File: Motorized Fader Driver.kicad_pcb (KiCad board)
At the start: 2 copper layers, 0 parts

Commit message: Update PCB
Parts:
- added C10: 100n, Capacitor_SMD:C_0402_1005Metric, B.Cu at (82.7, 38.4)
- added C11: 1u, Capacitor_SMD:C_0402_1005Metric, B.Cu at (79.8, 30.5)
- added C12: 100n, Capacitor_SMD:C_0402_1005Metric, B.Cu at (79.8, 32.5)
- added C13: 1u, Capacitor_SMD:C_0402_1005Metric, B.Cu at (79.8, 34.4)
- added C14: 100n, Capacitor_SMD:C_0402_1005Metric, B.Cu at (79.8, 36.4)
- added C15: 100n, Capacitor_SMD:C_0402_1005Metric, B.Cu at (79.8, 38.4)
- added C16: 100n, Capacitor_SMD:C_0402_1005Metric, B.Cu at (77.0, 30.5)
- added C17: 100n, Capacitor_SMD:C_0402_1005Metric, B.Cu at (77.0, 32.5)
- added C18: 100n, Capacitor_SMD:C_0402_1005Metric, B.Cu at (77.0, 34.4)
- added C19: 100n, Capacitor_SMD:C_0402_1005Metric, B.Cu at (77.0, 36.4)
- added C4: 15p, Capacitor_SMD:C_0402_1005Metric, B.Cu at (82.7, 30.5)
- added C5: 15p, Capacitor_SMD:C_0402_1005Metric, B.Cu at (82.7, 32.5)
- added C6: 10u, Capacitor_SMD:C_0805_2012Metric, B.Cu at (75.3, 49.6)
- added C7: 10u, Capacitor_SMD:C_0805_2012Metric, B.Cu at (75.3, 52.6)
- added C8: 100n, Capacitor_SMD:C_0402_1005Metric, B.Cu at (82.7, 34.4)
- added C9: 100n, Capacitor_SMD:C_0402_1005Metric, B.Cu at (82.7, 36.4)
- added J1: Conn_01x02, Connector_PinHeader_2.54mm:PinHeader_1x02_P2.54mm_Vertical, F.Cu at (110.5, 54.5)
- added J3: Conn_01x02, Connector_PinHeader_2.54mm:PinHeader_1x02_P2.54mm_Vertical, B.Cu at (89.0, 38.2)
- added R5: 1k, Resistor_SMD:R_0402_1005Metric, B.Cu at (82.7, 40.4)
- added R6: DNF, Resistor_SMD:R_0402_1005Metric, B.Cu at (82.7, 42.4)
- added R7: 1k, Resistor_SMD:R_0402_1005Metric, B.Cu at (82.7, 44.3)
- added R8: 27, Resistor_SMD:R_0402_1005Metric, B.Cu at (82.7, 46.3)
- added R9: 27, Resistor_SMD:R_0402_1005Metric, B.Cu at (82.7, 48.3)
- added U1: DRV8833PWP, Package_SO:HTSSOP-16-1EP_4.4x5mm_P0.65mm_EP3.4x5mm_Mask2.46x2.31mm_ThermalVias, B.Cu at (101.8, 48.0)
- added U4: NCP1117-3.3_SOT223, Package_TO_SOT_SMD:SOT-223-3_TabPin2, B.Cu at (32.5, 43.0)
- added U5: W25Q128JVS, Package_SO:SOIC-8_5.23x5.23mm_P1.27mm, B.Cu at (48.0, 45.0)
- added U6: RP2040, Package_DFN_QFN:QFN-56-1EP_7x7mm_P0.4mm_EP3.2x3.2mm_ThermalVias, B.Cu at (31.9, 32.4)
- added VR1: PSM60-081A-103B2, PSM60-081A-103B2:PSM60081A103B2, F.Cu at (110.1, 32.1)
- added Y2: ABM8-272-T3, Crystal:Crystal_SMD_3225-4Pin_3.2x2.5mm, B.Cu at (70.5, 50.3)
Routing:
- net Net-(J1-Pin_2): track 0.00 -> 14.4 mm
- net Net-(J1-Pin_1): track 0.00 -> 13.0 mm
- net /RP2040/GPIO6: track 0.00 -> 12.2 mm

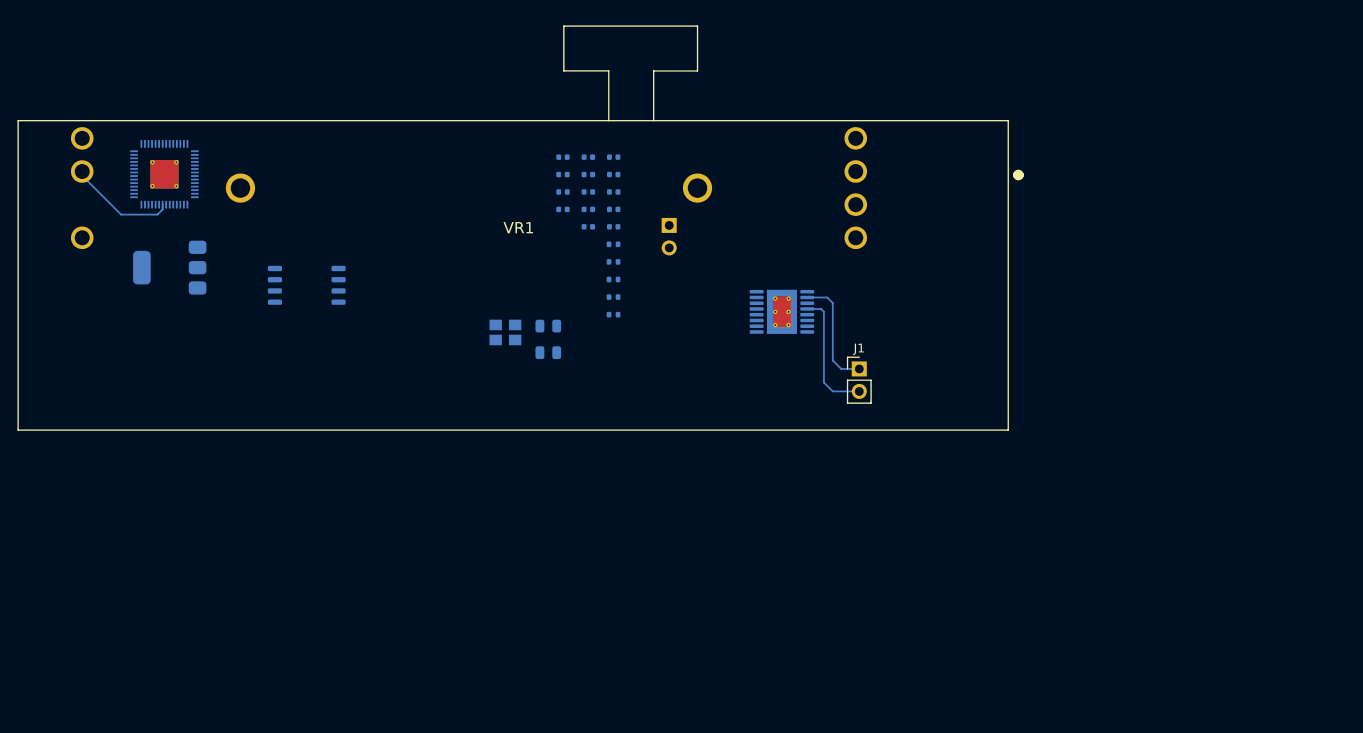
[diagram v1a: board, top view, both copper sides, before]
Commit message: Finish most of the schematic design
The majority of the schematic is in a pretty finalized state now. Also
some more work on the PCB has been done.
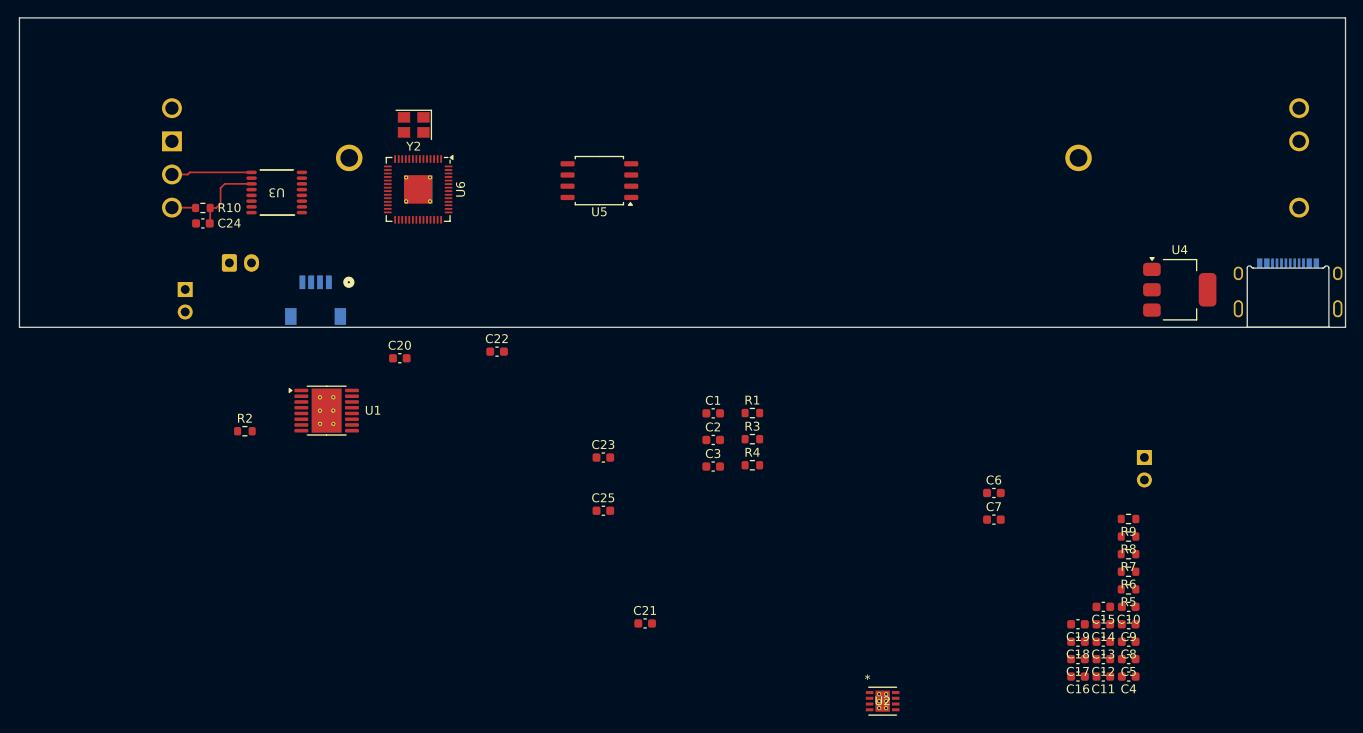
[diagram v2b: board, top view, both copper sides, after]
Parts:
- added C1: 2.2u, Capacitor_SMD:C_0603_1608Metric, F.Cu at (94.0, 59.5)
- added C2: 0.01u, Capacitor_SMD:C_0603_1608Metric, F.Cu at (94.0, 62.5)
- added C20: 0.1u, Capacitor_SMD:C_0603_1608Metric, F.Cu at (58.5, 53.2)
- added C21: 0.1u, Capacitor_SMD:C_0603_1608Metric, F.Cu at (86.3, 83.2)
- added C22: 0.1u, Capacitor_SMD:C_0603_1608Metric, F.Cu at (69.5, 52.5)
- added C23: 0.1u, Capacitor_SMD:C_0603_1608Metric, F.Cu at (81.5, 64.5)
- added C24: 100n, Capacitor_SMD:C_0603_1608Metric, F.Cu at (36.2, 38.0)
- added C25: 0.1u, Capacitor_SMD:C_0603_1608Metric, F.Cu at (81.5, 70.5)
- added C3: 10u, Capacitor_SMD:C_0603_1608Metric, F.Cu at (94.0, 65.5)
- added G***: LOGO, SparkFun-Qwiic:qwiic_6mm, B.Cu at (49.0, 42.0)
- added J2: Conn_I2C, Connector_SM04B_SRSS_TB:CONN_SM04B-SRSS-TB_JST, B.Cu at (49.0, 46.8)
- added J5: Conn_Mot_Pwr, Connector_JST:JST_EH_S2B-EH_1x02_P2.50mm_Horizontal, B.Cu at (39.2, 42.5)
- added J6: GSB1C4621DS1HR, GSB1C4621DS1HR:AMPHENOL_GSB1C4621DS1HR, B.Cu at (159.0, 47.6)
- added R1: 1M, Resistor_SMD:R_0603_1608Metric, F.Cu at (98.4, 59.5)
- added R10: 1k, Resistor_SMD:R_0603_1608Metric, F.Cu at (36.2, 36.2)
- added R2: 200m, Resistor_SMD:R_0603_1608Metric, F.Cu at (41.0, 61.5)
- added R3: 5.1k, Resistor_SMD:R_0603_1608Metric, F.Cu at (98.4, 62.4)
- added R4: 5.1k, Resistor_SMD:R_0603_1608Metric, F.Cu at (98.4, 65.3)
- added U2: TPS2115ADRBR, TPS2115ADRBR:DRB8_2P4X1P65, F.Cu at (113.1, 92.0)
- added U3: ADS1219IPWR, ADS1219IPWR:PW0016A_L, F.Cu at (44.6, 34.5)
- C10, C11, C12, C13, C14, C15, C16, C17, C18, C19, C4, C5, C8, C9: footprint Capacitor_SMD:C_0402_1005Metric -> Capacitor_SMD:C_0603_1608Metric; moved to F.Cu
- C6, C7: footprint Capacitor_SMD:C_0805_2012Metric -> Capacitor_SMD:C_0603_1608Metric; moved to F.Cu
- J1: value Conn_01x02 -> Conn_Mot; moved to B.Cu
- R5, R6, R7, R8, R9: footprint Resistor_SMD:R_0402_1005Metric -> Resistor_SMD:R_0603_1608Metric; moved to F.Cu
- U1, U4, U5, U6, Y2: moved to F.Cu
- VR1: value PSM60-081A-103B2 -> PSM01-081A-103B2; footprint PSM60-081A-103B2:PSM60081A103B2 -> PSM01-082A-103B2:PSM01081A103B2; moved to B.Cu
- moved U4 114.3 mm to (146.8, 45.5), turned to 0 degrees
- moved C11 82.7 mm to (138.1, 89.2)
- moved C16 82.7 mm to (135.2, 89.2)
- moved C4 82.7 mm to (141.0, 89.2)
- moved C17 80.0 mm to (135.2, 87.3)
- moved C12 80.0 mm to (138.1, 87.3)
- moved C5 80.0 mm to (141.0, 87.3)
- moved VR1 77.4 mm to (32.8, 28.7), turned to 180 degrees
- moved C18 77.3 mm to (135.2, 85.3)
- moved C13 77.3 mm to (138.1, 85.3)
- moved C8 77.3 mm to (141.0, 85.3)
- moved J1 76.8 mm to (34.2, 45.5), turned to 180 degrees
- moved C14 74.8 mm to (138.1, 83.3)
- moved C19 74.8 mm to (135.2, 83.3)
- moved C9 74.8 mm to (141.0, 83.3)
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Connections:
- net /RP2040/GPIO6 renamed /GPIO6
- U1 pad 1: unconnected-(U1-~{SLEEP}-Pad1) -> /RP2040/GPIO7
- U1 pad 10: unconnected-(U1-BIN2-Pad10) -> /RP2040/GPIO5
- U1 pad 11: unconnected-(U1-VCP-Pad11) -> Net-(U1-VCP)
- U1 pad 13: Net-(U1-GND-Pad13) -> GND
- U1 pad 14: unconnected-(U1-VINT-Pad14) -> Net-(U1-VINT)
- U1 pad 17: Net-(U1-GND-Pad13) -> GND
- U1 pad 3: unconnected-(U1-AISEN-Pad3) -> Net-(U1-AISEN)
- U1 pad 5: unconnected-(U1-BOUT2-Pad5) -> Net-(J1-Pin_2)
- U1 pad 6: unconnected-(U1-BISEN-Pad6) -> Net-(U1-AISEN)
- U1 pad 7: unconnected-(U1-BOUT1-Pad7) -> Net-(J1-Pin_1)
- U1 pad 8: unconnected-(U1-~{FAULT}-Pad8) -> /RP2040/GPIO8
- U1 pad 9: unconnected-(U1-BIN1-Pad9) -> /RP2040/GPIO4
- U4 pad 2: +3V3 -> Net-(U2-IN1)
- U6 pad 11: unconnected-(U6-GPIO8-Pad11) -> /RP2040/GPIO8
- U6 pad 2: unconnected-(U6-GPIO0-Pad2) -> /CONN_SDA
- U6 pad 3: unconnected-(U6-GPIO1-Pad3) -> /CONN_SCL
- U6 pad 38: /RP2040/ADC0 -> unconnected-(U6-GPIO26_ADC0-Pad38)
- U6 pad 4: unconnected-(U6-GPIO2-Pad4) -> /I2C_SDA
- U6 pad 5: unconnected-(U6-GPIO3-Pad5) -> /I2C_SCL
- U6 pad 9: unconnected-(U6-GPIO7-Pad9) -> /RP2040/GPIO7
- VR1 pad B2: /RP2040/ADC0 -> Net-(VR1-WIPER_2)
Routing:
- net Net-(J1-Pin_2): track 14.4 -> 0.00 mm
- net Net-(J1-Pin_1): track 13.0 -> 0.49 mm
- net /GPIO6: track 12.2 -> 0.00 mm
- net +3V3: track 0.00 -> 9.10 mm
- net Net-(U3-AIN0): track 0.00 -> 8.60 mm
- net Net-(VR1-WIPER_2): track 0.00 -> 2.69 mm
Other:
- board outline added: 150 x 35 mm

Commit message: Finish routing most of the PCB
The PCB should work now for the most part. Also fixes some miscellaneous
schematic things and swaps out a few components.
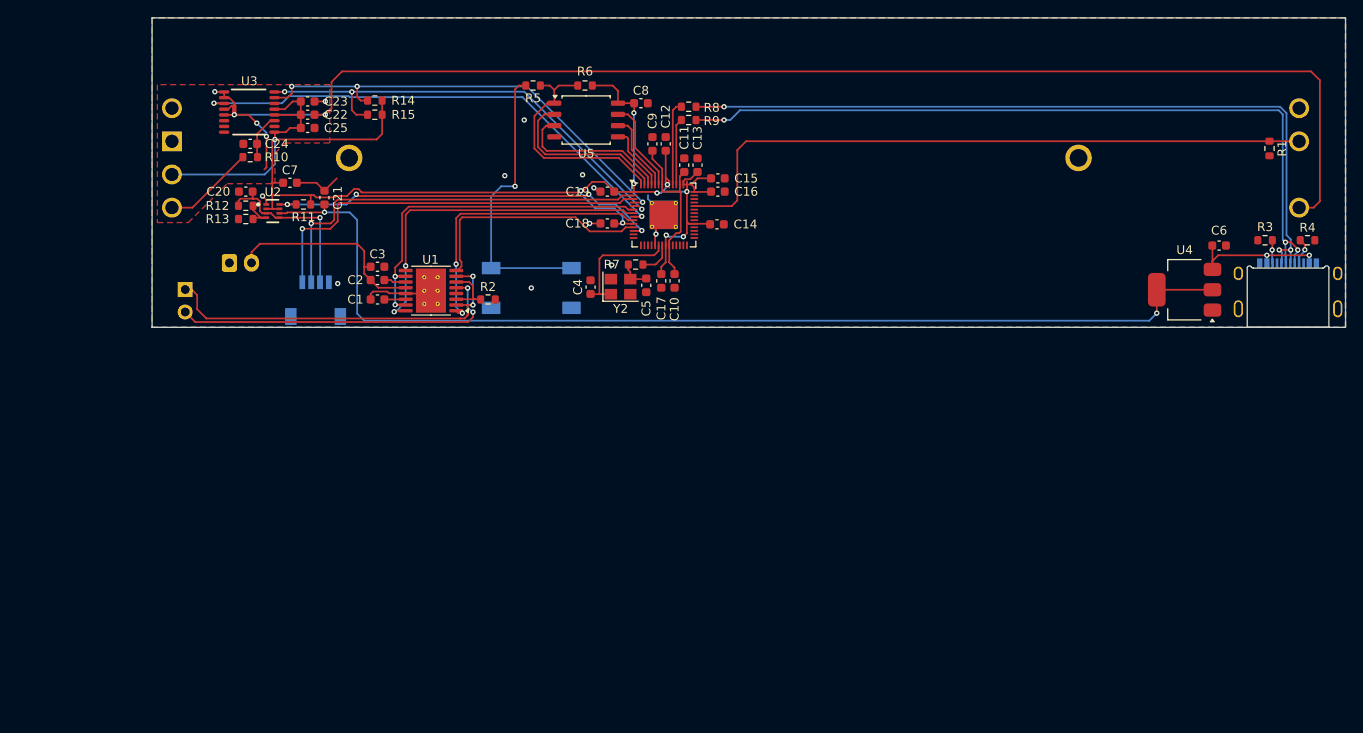
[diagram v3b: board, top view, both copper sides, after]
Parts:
- removed J3: Conn_01x02, Connector_PinHeader_2.54mm:PinHeader_1x02_P2.54mm_Vertical
- added NT1: NetTie_2, NetTie:NetTie-2_SMD_Pad0.5mm, F.Cu at (39.8, 25.2)
- added R11: R_Small, Resistor_SMD:R_0603_1608Metric, F.Cu at (47.6, 35.8)
- added R12: R_Small, Resistor_SMD:R_0603_1608Metric, F.Cu at (41.1, 36.0)
- added R13: R_Small, Resistor_SMD:R_0603_1608Metric, F.Cu at (41.1, 37.5)
- added R14: 4.7k, Resistor_SMD:R_0603_1608Metric, F.Cu at (55.7, 24.1)
- added R15: 4.7k, Resistor_SMD:R_0603_1608Metric, F.Cu at (55.7, 25.7)
- added SW1: TS04-66-70-BK-160-SMT, TS04_66_70_BK_160_SMT2:SW_TS04-66-70-BK-160-SMT, B.Cu at (73.4, 45.3)
- J1: value Conn_Mot -> Motor
- J5: value Conn_Mot_Pwr -> Motor_Power
- U2: value TPS2115ADRBR -> TPS2116DRLR; footprint TPS2115ADRBR:DRB8_2P4X1P65 -> TPS2116DRLR:DRL0008A-MFG
- moved U2 88.5 mm to (44.2, 36.6)
- moved C7 88.3 mm to (46.1, 33.4)
- moved R5 88.2 mm to (73.6, 22.4)
- moved R6 82.5 mm to (79.5, 22.4)
- moved C8 82.2 mm to (85.8, 24.4), turned to 0 degrees
- moved C9 76.5 mm to (87.1, 29.0), turned to 90 degrees
- moved C12 76.5 mm to (88.6, 29.0), turned to 90 degrees
- moved C4 75.1 mm to (80.1, 45.2), turned to 90 degrees
- moved C11 74.8 mm to (90.7, 31.4), turned to 90 degrees
- moved C19 72.3 mm to (82.0, 34.4)
- moved C18 71.2 mm to (82.0, 38.0)
- moved C13 70.8 mm to (92.2, 31.4), turned to 90 degrees
- moved R8 69.6 mm to (91.2, 24.8)
- moved C5 69.0 mm to (86.4, 45.0), turned to -90 degrees
- moved C16 68.3 mm to (94.5, 34.4), turned to 0 degrees
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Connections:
- C21 pad 1: Net-(U2-IN1) -> Net-(U2-VIN2)
- C22 pad 1: GND -> GNDA
- C24 pad 2: GND -> GNDA
- C25 pad 2: GND -> GNDA
- R1 pad 1: /GPIO6 -> /TOUCH
- R8 pad 1: /RP2040/USB_D+ -> /USB_D+
- R9 pad 1: /RP2040/USB_D- -> /USB_D-
- U1 pad 10: /RP2040/GPIO5 -> /RP2040/GPIO4
- U1 pad 15: /RP2040/GPIO5 -> /RP2040/GPIO4
- U1 pad 16: /RP2040/GPIO4 -> /RP2040/GPIO5
- U1 pad 9: /RP2040/GPIO4 -> /RP2040/GPIO5
- U2 pad 1: unconnected-(U2-STAT-Pad1) -> GND
- U2 pad 2: unconnected-(U2-D0-Pad2) -> +3V3
- U2 pad 3: unconnected-(U2-D1-Pad3) -> /CONN_PWRIN
- U2 pad 4: unconnected-(U2-ILIM-Pad4) -> Net-(U2-PR1)
- U2 pad 5: GND -> /CONN_PWRIN
- U2 pad 6: /CONN_PWRIN -> Net-(U2-VIN2)
- U2 pad 8: Net-(U2-IN1) -> /PWR_STAT
- U3 pad 3: unconnected-(U3-RESET_N-Pad3) -> /ADC_RESET
- U3 pad 5: GND -> GNDA
- U3 pad 8: GND -> GNDA
- U4 pad 2: Net-(U2-IN1) -> Net-(U2-VIN2)
- U6 pad 12: unconnected-(U6-GPIO9-Pad12) -> /PWR_STAT
- U6 pad 38: unconnected-(U6-GPIO26_ADC0-Pad38) -> /TOUCH
- U6 pad 8: /GPIO6 -> /ADC_RESET
- VR1 pad B3: GND -> GNDA
- VR1 pad T1: /GPIO6 -> /TOUCH
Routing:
- net GNDA: track 0.00 -> 154.5 mm, vias 0 -> 4
- net +3V3: track 9.10 -> 161.3 mm, vias 0 -> 10
- net Net-(U2-VIN2): track 0.00 -> 120.8 mm, vias 0 -> 2
- net /USB_D-: track 0.00 -> 87.4 mm, vias 0 -> 3
- net /USB_D+: track 0.00 -> 87.2 mm, vias 0 -> 3
- net /TOUCH: track 0.00 -> 74.8 mm
- net /ADC_RESET: track 0.00 -> 56.5 mm, vias 0 -> 2
- net /I2C_SCL: track 0.00 -> 52.2 mm, vias 0 -> 3
- net /I2C_SDA: track 0.00 -> 51.7 mm, vias 0 -> 3
- net /CONN_SCL: track 0.00 -> 46.0 mm, vias 0 -> 1
- net /CONN_SDA: track 0.00 -> 45.5 mm, vias 0 -> 1
- net /PWR_STAT: track 0.00 -> 45.3 mm, vias 0 -> 4
- net Net-(J1-Pin_1): track 0.49 -> 43.2 mm, vias 0 -> 2
- net /RP2040/GPIO4: track 0.00 -> 40.0 mm, vias 0 -> 2
- net /RP2040/GPIO5: track 0.00 -> 39.6 mm, vias 0 -> 2
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- added copper zone on B.Cu, net GND
- added copper zone on F.Cu, net GND
- added copper zone on F.Cu, net GNDA
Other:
- board size 150 x 35 mm -> 135 x 35 mm

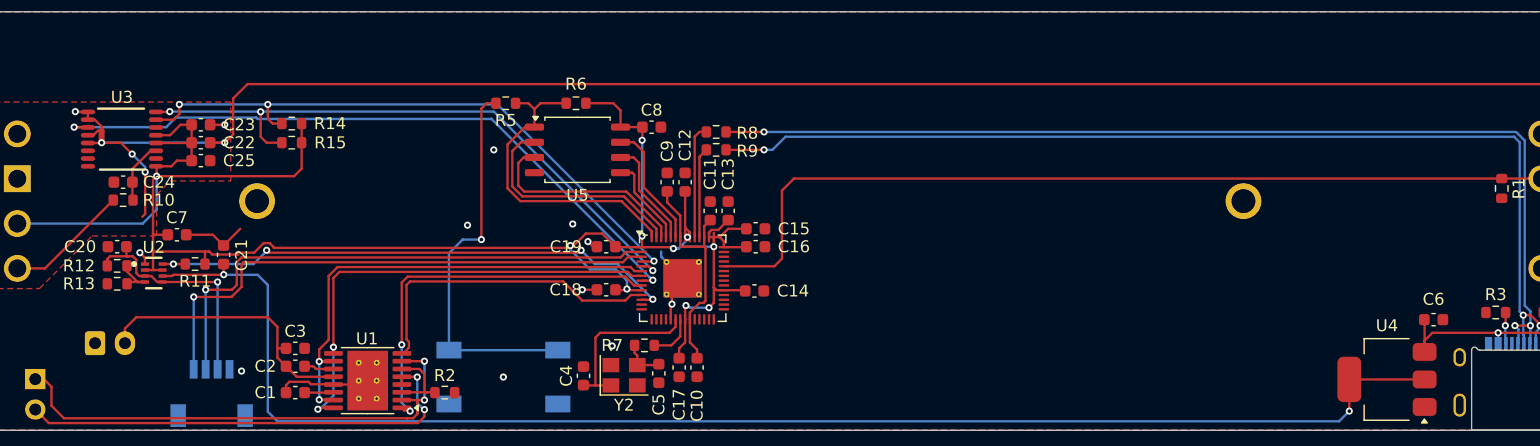
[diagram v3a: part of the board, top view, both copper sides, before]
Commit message: Route more things and add LCSC part numbers for things
The LCSC part numbers allow for JLCPCB's PCBA tool to find the parts.
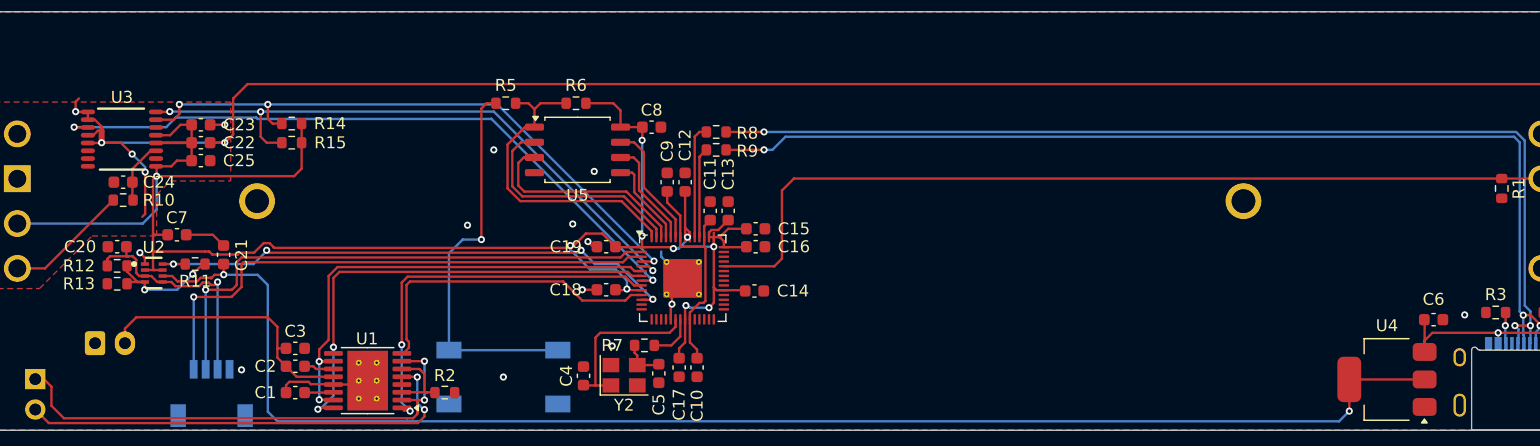
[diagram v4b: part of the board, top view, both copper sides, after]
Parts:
- C2: value 0.01u -> 10n
- C20, C21, C22, C23, C25: value 0.1u -> 100n
- R11: value R_Small -> 10k
- R12: value R_Small -> 5k
- R13: value R_Small -> 4k
- R6: value DNF -> DNP
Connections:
- R11 pad 1: +3V3 -> Net-(U2-PR1)
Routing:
- net Net-(U2-PR1): track 3.89 -> 10.5 mm, vias 0 -> 2
- net +3V3: track 161.3 -> 160.2 mm
- net GND: track 26.0 -> 25.2 mm, vias 11 -> 14
- net Net-(U2-VIN2): track 120.8 -> 121.3 mm
- net (no net): vias 1 -> 0
